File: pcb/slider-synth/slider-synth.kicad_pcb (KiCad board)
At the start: 2 copper layers, 47 parts, among them J1 USB4105, J2 PJ-325C5-G, J3 Conn_01x01_Pin, J4 Conn_01x01_Pin, SW1 SW_SPST, SW2 SW_SPST, SW3 RotaryEncoder_Switch, U1 ESP32-S3-WROOM-2, U2 LM3940IMPX-3.3/NOPB, U32 MCP4922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

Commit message: price optimizations
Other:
- board outline added: 100 x 80.6 mm
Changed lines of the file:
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@@
 		)
+	)
+	(gr_rect
+		(start 100.6 43.7)
+		(end 200.6 124.3)
+		(stroke
+			(width 0.05)
+			(type solid)
+		)
+		(fill no)
+		(layer "Edge.Cuts")
 	)
 	(embedded_fonts no)

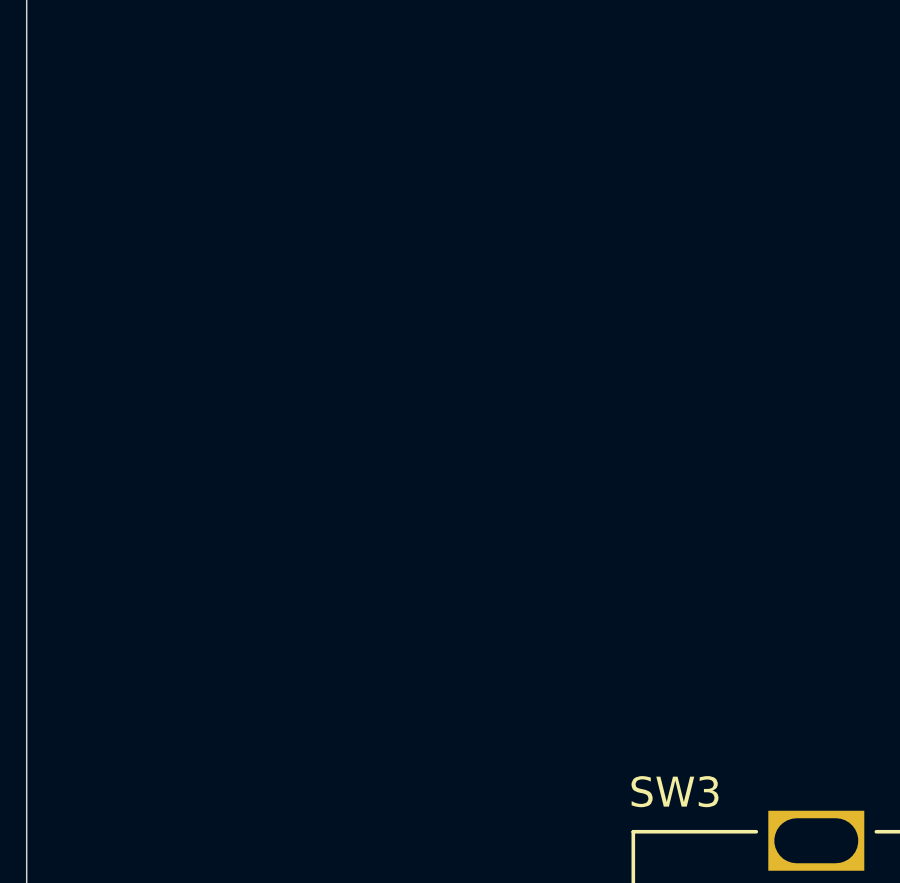
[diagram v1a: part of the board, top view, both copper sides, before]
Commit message: add fsr and linear pot
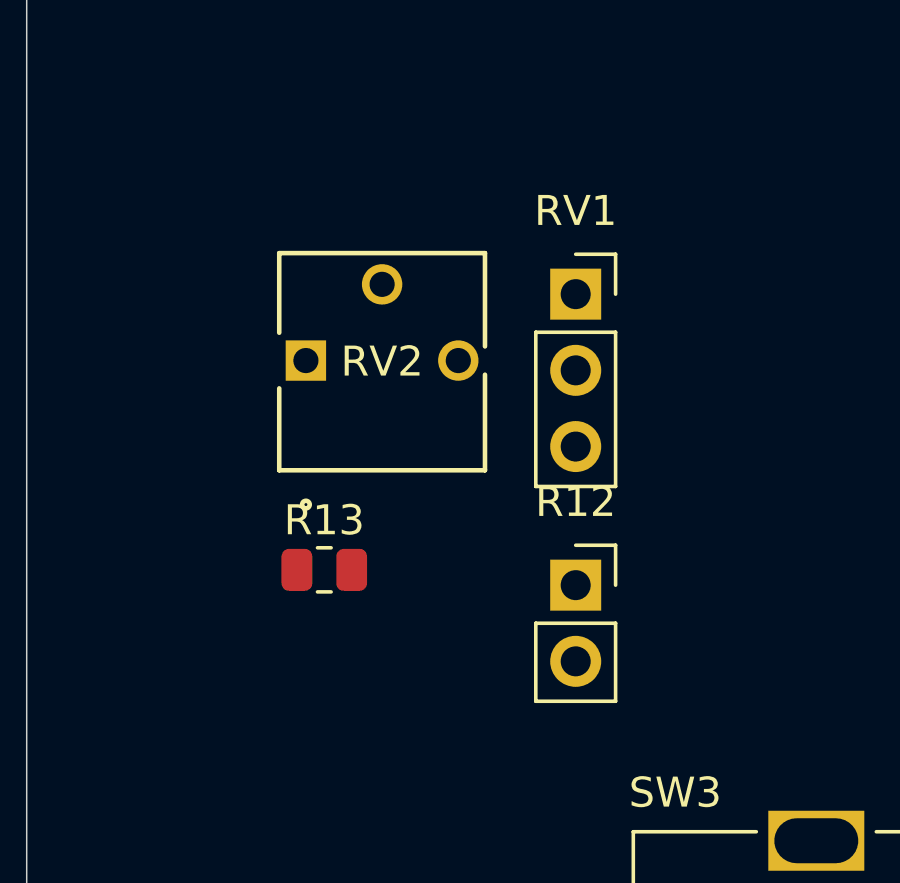
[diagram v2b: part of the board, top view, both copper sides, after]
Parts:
- added R12: Force Sensitive Resistor 500mm, Connector_PinSocket_2.54mm:PinSocket_1x02_P2.54mm_Vertical, F.Cu at (118.9, 89.1)
- added R13: 10kΩ, Resistor_SMD:R_0805_2012Metric, F.Cu at (110.5, 88.5)
- added RV1: SEN-08681, Connector_PinSocket_2.54mm:PinSocket_1x03_P2.54mm_Vertical, F.Cu at (118.9, 79.4)
- added RV2: 3362P-100kΩ, 2_udu_lib:POT_3362P, F.Cu at (109.9, 81.6)
- C3: value 33μF -> 47μF
- C42, C44: value 0.05μF -> 33nF
- C43, C45: value 250μF -> 47μF
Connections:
- U1 pad 21: unconnected-(U1-IO13-Pad21) -> LinearPot

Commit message: footprints and routing
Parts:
- removed D2: LED, LED_THT:LED_D5.0mm
- removed R7: 330Ω, Resistor_SMD:R_0805_2012Metric
- moved D3 92.5 mm to (106.4, 131.9), turned to 180 degrees
- moved D4 82.2 mm to (113.5, 131.9), turned to 180 degrees
- moved J2 74.8 mm to (127.8, 113.3)
- moved D5 71.8 mm to (120.7, 131.9), turned to 180 degrees
- moved U1 62.9 mm to (188.2, 124.3), turned to -90 degrees
- moved D6 61.5 mm to (127.8, 131.9), turned to 180 degrees
- moved RV2 50.6 mm to (145.7, 117.3)
- moved R3 50.0 mm to (187.1, 113.0)
- moved C48 49.0 mm to (134.4, 130.0), turned to 90 degrees
- moved SW1 47.6 mm to (165.6, 121.4)
- moved SW2 46.9 mm to (165.6, 129.3)
- moved R4 45.3 mm to (182.9, 113.0)
- moved C47 45.1 mm to (145.4, 132.6)
- moved C49 44.9 mm to (134.0, 125.0), turned to 90 degrees
- moved U32 43.4 mm to (139.6, 117.5)
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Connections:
- U1 pad 10: LED4 -> unconnected-(U1-IO17-Pad10)
- U1 pad 15: RotA -> unconnected-(U1-IO3-Pad15)
- U1 pad 22: LED1 -> unconnected-(U1-IO14-Pad22)
- U1 pad 23: unconnected-(U1-IO21-Pad23) -> RotA
- U1 pad 24: unconnected-(U1-IO47-Pad24) -> RotB
- U1 pad 25: unconnected-(U1-IO48-Pad25) -> RotSw
- U1 pad 32: unconnected-(U1-MTCK/IO39-Pad32) -> LED1
- U1 pad 33: unconnected-(U1-MTDO/IO40-Pad33) -> LED2
- U1 pad 34: unconnected-(U1-MTDI/IO41-Pad34) -> LED3
- U1 pad 35: unconnected-(U1-MTMS/IO42-Pad35) -> LED4
- U1 pad 4: RotB -> unconnected-(U1-IO4-Pad4)
- U1 pad 5: RotSw -> unconnected-(U1-IO5-Pad5)
- U1 pad 8: LED2 -> unconnected-(U1-IO15-Pad8)
- U1 pad 9: LED3 -> unconnected-(U1-IO16-Pad9)
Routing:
- net VDD: track 0.00 -> 113.3 mm, vias 0 -> 4
- net LED1: track 0.00 -> 83.6 mm, vias 0 -> 1
- net LinearPot: track 0.00 -> 81.2 mm, vias 0 -> 3
- net RotA: track 0.00 -> 79.1 mm, vias 0 -> 1
- net LED2: track 0.00 -> 78.0 mm, vias 0 -> 1
- net RotB: track 0.00 -> 76.3 mm, vias 0 -> 1
- net LED3: track 0.00 -> 72.5 mm, vias 0 -> 2
- net LED4: track 0.00 -> 65.8 mm, vias 0 -> 2
- net RotSw: track 0.00 -> 62.4 mm, vias 0 -> 2
- net GND: track 0.00 -> 51.2 mm, vias 0 -> 16
- net 3v3: track 0.00 -> 49.8 mm
- net CS: track 0.00 -> 45.5 mm, vias 0 -> 4
- net SCK: track 0.00 -> 42.6 mm, vias 0 -> 2
- net SDI: track 0.00 -> 41.7 mm, vias 0 -> 2
- net 5v: track 0.00 -> 37.0 mm
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- added copper zone on B.Cu, net GND
- added copper zone on F.Cu, net GND
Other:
- board size 100 x 80.6 mm -> 94.6 x 25 mm

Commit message: prod files, cad, and cool silkscreen
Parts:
- added G***: LOGO, 1_udu_lib:slider_synth_back, B.Cu at (145.5, 125.6)

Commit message: Add bom, readme/journal stuff
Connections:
- R12 pad 2: Net-(R12-Pad2) -> FSR
- R13 pad 2: Net-(R12-Pad2) -> FSR
- U1 pad 31: unconnected-(U1-IO38-Pad31) -> FSR
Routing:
- net FSR: track 0.00 -> 105.3 mm, vias 0 -> 2
- net Net-(R12-Pad2): track 20.6 -> 0.00 mm, vias 1 -> 0

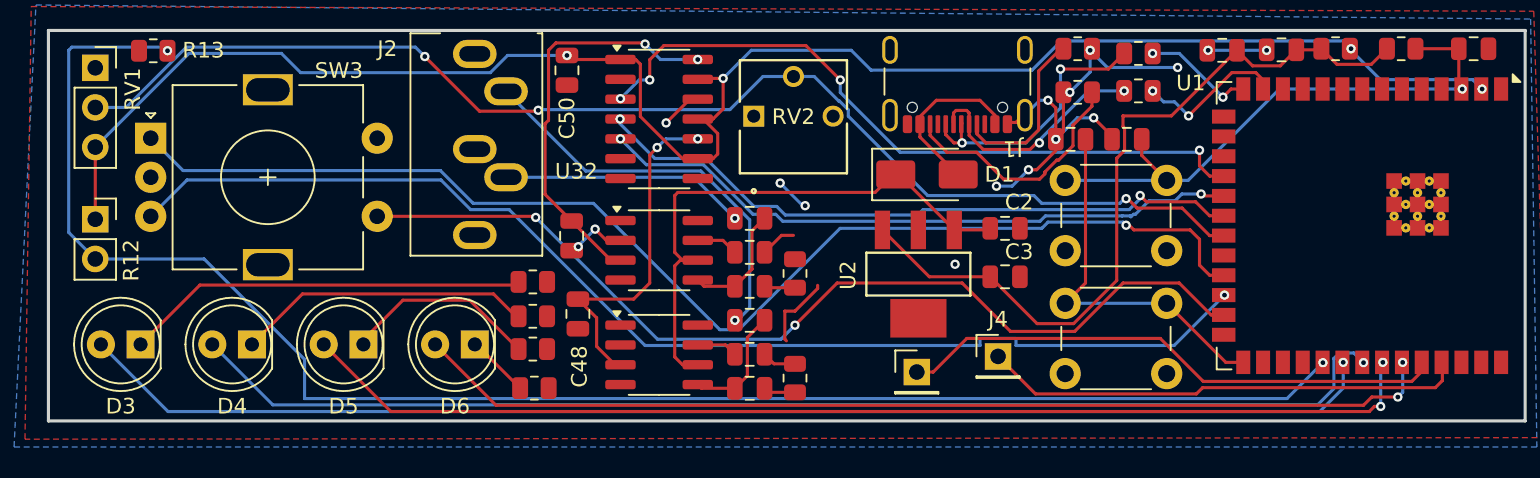
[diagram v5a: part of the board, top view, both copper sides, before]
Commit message: move io38 to io4, but did not update prod files
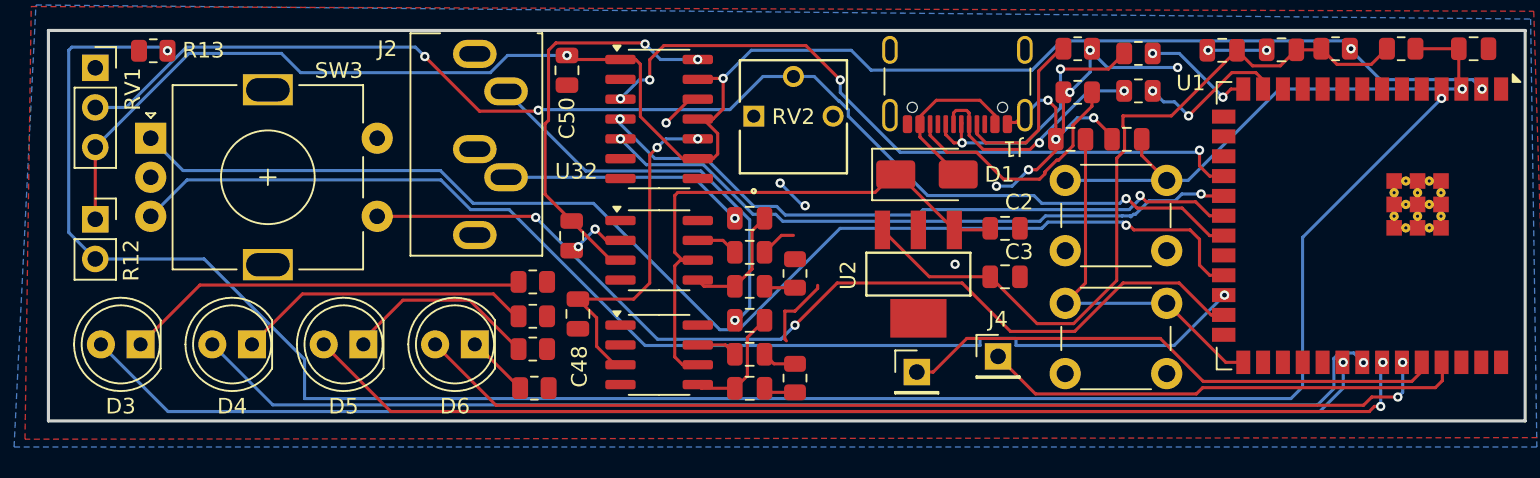
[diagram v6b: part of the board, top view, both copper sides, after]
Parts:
- C46, C47: value 0.05μF -> 47nF
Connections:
- U1 pad 31: FSR -> unconnected-(U1-IO38-Pad31)
- U1 pad 4: unconnected-(U1-IO4-Pad4) -> FSR
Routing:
- net FSR: track 105.3 -> 125.5 mm
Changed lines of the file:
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@@
 	(net 41 "unconnected-(U1-IO46-Pad16)")
 	(net 42 "unconnected-(U1-IO2-Pad38)")
-	(net 43 "unconnected-(U1-IO4-Pad4)")
+	(net 43 "unconnected-(U1-IO38-Pad31)")
 	(net 44 "FSR")
 	(net 45 "unconnected-(U1-IO18-Pad11)")
@@
 			)
 		)
-		(property "Value" "0.05μF"
+		(property "Value" "47nF"
 			(at 0 1.68 0)
 			(layer "F.Fab")
@@
 			(size 1.5 0.9)
 			(layers "F.Cu" "F.Mask" "F.Paste")
-			(net 43 "unconnected-(U1-IO4-Pad4)")
+			(net 44 "FSR")
 			(pinfunction "IO4")
 			(pintype "bidirectional")
@@
 			(size 1.5 0.9)
 			(layers "F.Cu" "F.Mask" "F.Paste")
-			(net 44 "FSR")
+			(net 43 "unconnected-(U1-IO38-Pad31)")
 			(pinfunction "IO38")
 			(pintype "bidirectional")
@@
 			)
 		)
-		(property "Value" "0.05μF"
+		(property "Value" "47nF"
 			(at 0 1.68 0)
 			(layer "F.Fab")
@@
 		(width 0.2)
 		(layer "F.Cu")
-		(net 44)
+		(net 43)
 	)
 	(via
@@
 	)
 	(via
-		(at 182.1 133.1)
+		(at 189.7 116.18)
 		(size 0.6)
 		(drill 0.3)
@@
 	)
 	(segment
+		(start 116.9 135.399)
+		(end 180.051 135.399)
+		(width 0.2)
+		(layer "B.Cu")
+		(net 44)
+	)
+	(segment
+		(start 110.465333 126.46)
+		(end 116.9 132.894667)
+		(width 0.2)
+		(layer "B.Cu")
+		(net 44)
+	)
+	(segment
 		(start 103.5 126.46)
 		(end 101.8 124.76)
@@
 	)
 	(segment
-		(start 179.801 135.399)
-		(end 116.9 135.399)
+		(start 180.051 135.399)
+		(end 180.8 134.65)
 		(width 0.2)
 		(layer "B.Cu")
@@
 	)
 	(segment
-		(start 110.465333 126.46)
-		(end 103.5 126.46)
+		(start 180.8 134.65)
+		(end 180.8 125.08)
 		(width 0.2)
 		(layer "B.Cu")
@@
 	)
 	(segment
-		(start 182.1 133.1)
-		(end 179.801 135.399)
+		(start 180.8 125.08)
+		(end 189.7 116.18)
 		(width 0.2)
 		(layer "B.Cu")
@@
 	)
 	(segment
-		(start 116.9 132.894667)
+		(start 103.5 126.46)
 		(end 110.465333 126.46)
 		(width 0.2)
@@
 	)
 	(segment
-		(start 116.9 135.399)
-		(end 116.9 132.894667)
+		(start 116.9 132.894667)
+		(end 116.9 135.399)
 		(width 0.2)
 		(layer "B.Cu")
